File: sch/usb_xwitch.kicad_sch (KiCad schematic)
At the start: 65 parts, among them J1 USB3_A, J2 USB3_A, J3 USB3_A, J4 USB3_A, J5 USB3_A, J6 USB3_A, J7 USB3_A, J8 Conn_02x05_Odd_Even, J9 C65114, K1 Relay_DPDT_Panasonic_AGQ200A4H, K2 Relay_DPDT_Panasonic_AGQ200A4H, K3 Relay_DPDT_Panasonic_AGQ200A4H, Q1 2N7002P, Q2 2N7002P, Q3 2N7002P, SW1 C2689642, U1 Pico

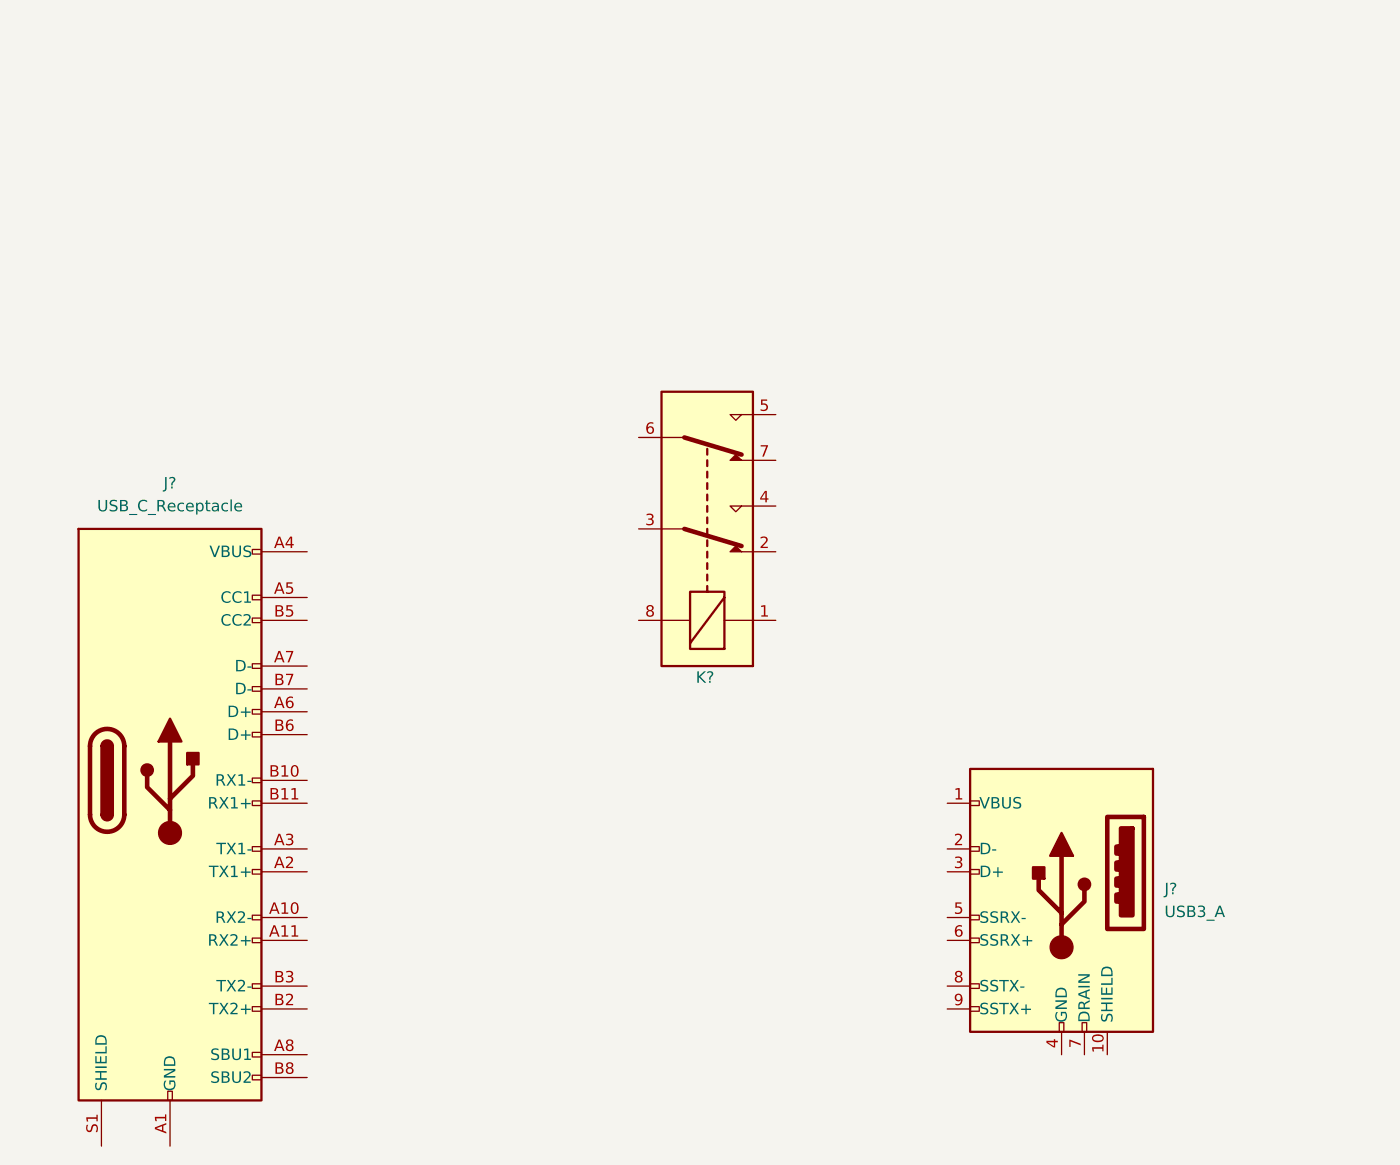
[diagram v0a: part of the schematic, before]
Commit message: added usb2 usb3 mux in sch
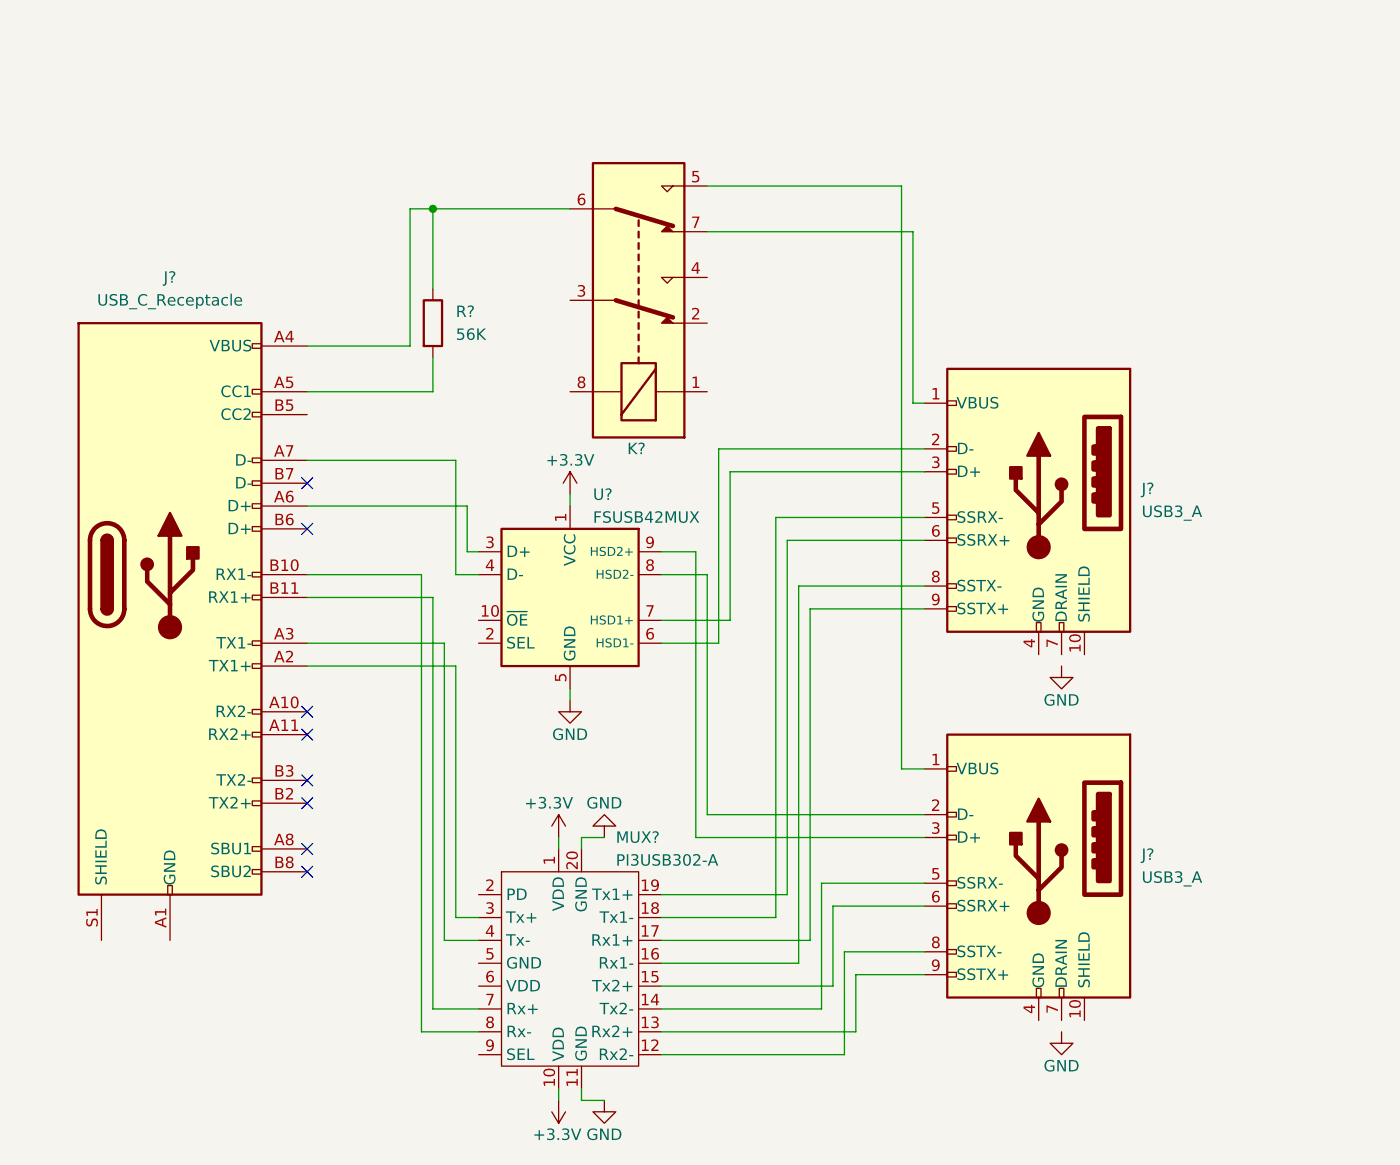
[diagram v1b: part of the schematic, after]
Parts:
- added J?: USB3_A, usb_xwitch:USB3_A_AdamTech_USB-A3-S-RA, symbol Connector:USB3_A
- added MUX?: PI3USB302-A, USB_MUX_DEMUX_PI3USB302-A:USB_MUX_DEMUX_PI3USB302-A, symbol usb_xwitch:PI3USB302-A
- added R?: 56K, symbol Device:R
- added U?: FSUSB42MUX, Package_SO:MSOP-10_3x3mm_P0.5mm, symbol Interface_USB:FSUSB42MUX
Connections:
- net +3V3: now also MUX?.1 (VDD), MUX?.10 (VDD), U?.1 (VCC)
- net GND: now also MUX?.11 (GND), MUX?.20 (GND), U?.5 (GND)
- net at K?.5: now also J?.1 (VBUS)
- net at K?.6: now also J?.A4 (VBUS), J?.A9 (VBUS), J?.B4 (VBUS), J?.B9 (VBUS), R?.1
- net at K?.7: now also J?.1 (VBUS)
- net at J?.A2 (TX1+): now also MUX?.3 (Tx+)
- net at J?.A3 (TX1-): now also MUX?.4 (Tx-)
- net at J?.A5 (CC1): now also R?.2
- net at J?.A6 (D+): now also U?.3 (D+)
- net at J?.A7 (D-): now also U?.4 (D-)
- net at J?.B10 (RX1-): now also MUX?.8 (Rx-)
- net at J?.B11 (RX1+): now also MUX?.7 (Rx+)
- net at J?.2 (D-): now also U?.6 (HSD1-)
- net at J?.3 (D+): now also U?.7 (HSD1+)
- net at J?.5 (SSRX-): now also MUX?.18 (Tx1-)
- net at J?.6 (SSRX+): now also MUX?.19 (Tx1+)
- net at J?.8 (SSTX-): now also MUX?.16 (Rx1-)
- net at J?.9 (SSTX+): now also MUX?.17 (Rx1+)
- new net: J?.2 (D-), U?.8 (HSD2-)
- new net: J?.3 (D+), U?.9 (HSD2+)
- new net: J?.5 (SSRX-), MUX?.14 (Tx2-)
- new net: J?.6 (SSRX+), MUX?.15 (Tx2+)
- new net: J?.8 (SSTX-), MUX?.12 (Rx2-)
- new net: J?.9 (SSTX+), MUX?.13 (Rx2+)
- no-connect marks 37 -> 45
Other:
- moved on the sheet: J?, K?

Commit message: updated usb mux wiring
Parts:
- added R? (x3): 0R, Resistor_SMD:R_0603_1608Metric_Pad0.98x0.95mm_HandSolder, symbol Device:R
- R?: footprint (none) -> Resistor_SMD:R_0402_1005Metric_Pad0.72x0.64mm_HandSolder; LCSC (none) -> C25796
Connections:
- net +3V3: now also MUX?.6 (VDD)
- net +5V: now also K?.1
- net GND: now also J?.A1 (GND), J?.A12 (GND), J?.B1 (GND), J?.B12 (GND), K?.3, MUX?.5 (GND), R?.1
- net PD-A: now also MUX?.2 (PD)
- net RL1: now also K?.8
- net SEL-A: now also MUX?.9 (SEL)
- net VBUS_1_1: now also J?.1 (VBUS), K?.7
- net VBUS_1_2: now also J?.1 (VBUS), K?.5
- net at K?.2: now also J?.4 (GND), J?.7 (DRAIN), R?.2
- net at K?.4: now also J?.4 (GND), J?.7 (DRAIN), R?.2
- net at J?.S1 (SHIELD): now also R?.2
- net at J?.10 (SHIELD): now also R?.1 (x2)
- no-connect marks 45 -> 46
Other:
- moved on the sheet: J6, J7, K3

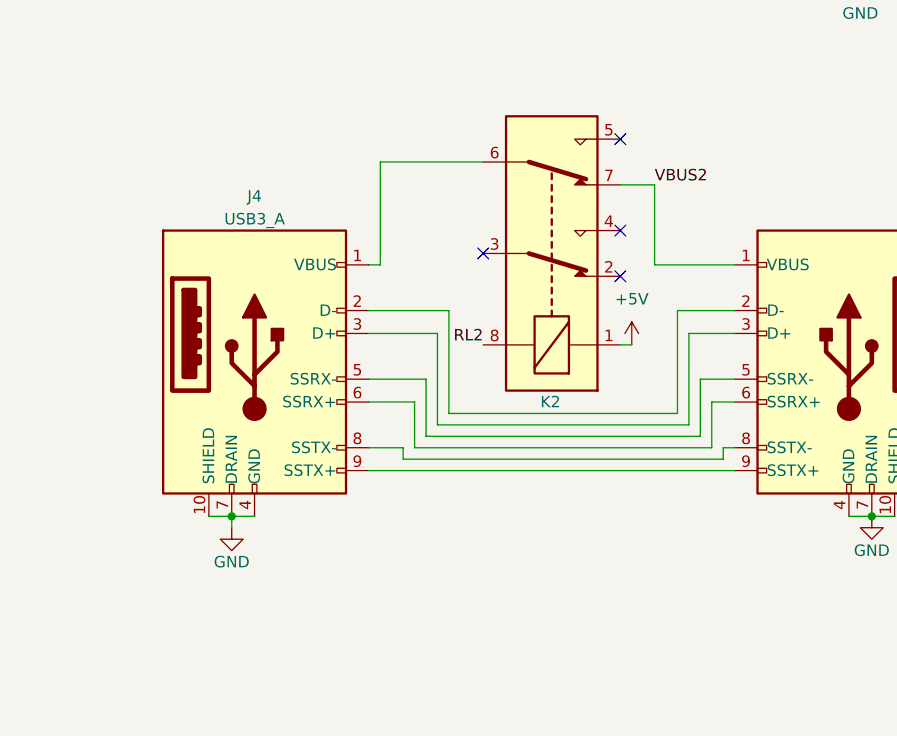
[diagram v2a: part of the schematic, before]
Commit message: added shouhan typec in lib
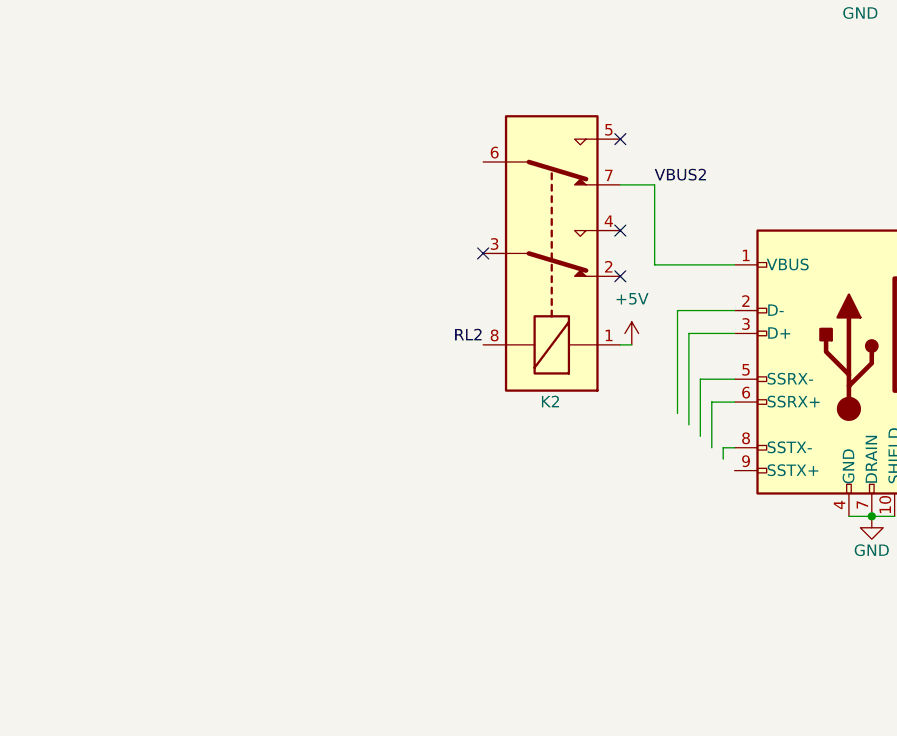
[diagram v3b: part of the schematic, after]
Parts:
- removed J4: USB3_A, usb_xwitch:USB3_A_AdamTech_USB-A3-S-RA, symbol Connector:USB3_A
- J?: footprint Connector_USB:USB_C_Receptacle_Amphenol_12401548E4-2A -> usb_xwitch:USB_TypeC_24Pin_ShouHan
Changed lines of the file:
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@@
   (junction (at 154.94 76.2) (diameter 0) (color 0 0 0 0)
   )
-  (junction (at 190.5 218.44) (diameter 0) (color 0 0 0 0)
-  )
   (junction (at 71.12 38.1) (diameter 0) (color 0 0 0 0)
   )
@@
     (stroke (width 0) (type default) (color 0 0 0 0))
   )
-  (wire (pts (xy 212.09 209.55) (xy 212.09 203.2))
-    (stroke (width 0) (type default) (color 0 0 0 0))
-  )
   (wire (pts (xy 104.14 265.43) (xy 104.14 259.08))
     (stroke (width 0) (type default) (color 0 0 0 0))
@@
     (stroke (width 0) (type default) (color 0 0 0 0))
   )
-  (wire (pts (xy 213.36 208.28) (xy 241.3 208.28))
-    (stroke (width 0) (type default) (color 0 0 0 0))
-  )
   (wire (pts (xy 237.49 77.47) (xy 257.81 77.47))
     (stroke (width 0) (type default) (color 0 0 0 0))
@@
     (stroke (width 0) (type default) (color 0 0 0 0))
   )
-  (wire (pts (xy 212.09 203.2) (xy 205.74 203.2))
-    (stroke (width 0) (type default) (color 0 0 0 0))
-  )
   (wire (pts (xy 95.25 252.73) (xy 95.25 208.28))
     (stroke (width 0) (type default) (color 0 0 0 0))
@@
     (stroke (width 0) (type default) (color 0 0 0 0))
   )
-  (wire (pts (xy 205.74 205.74) (xy 210.82 205.74))
-    (stroke (width 0) (type default) (color 0 0 0 0))
-  )
   (wire (pts (xy 176.53 86.36) (xy 171.45 86.36))
     (stroke (width 0) (type default) (color 0 0 0 0))
@@
     (stroke (width 0) (type default) (color 0 0 0 0))
   )
-  (wire (pts (xy 245.11 212.09) (xy 209.55 212.09))
-    (stroke (width 0) (type default) (color 0 0 0 0))
-  )
   (wire (pts (xy 101.6 251.46) (xy 113.03 251.46))
     (stroke (width 0) (type default) (color 0 0 0 0))
@@
     (stroke (width 0) (type default) (color 0 0 0 0))
   )
-  (wire (pts (xy 209.55 212.09) (xy 209.55 210.82))
-    (stroke (width 0) (type default) (color 0 0 0 0))
-  )
   (wire (pts (xy 151.13 60.96) (xy 148.59 60.96))
     (stroke (width 0) (type default) (color 0 0 0 0))
@@
     (stroke (width 0) (type default) (color 0 0 0 0))
   )
-  (wire (pts (xy 213.36 198.12) (xy 213.36 208.28))
-    (stroke (width 0) (type default) (color 0 0 0 0))
-  )
   (wire (pts (xy 68.58 194.31) (xy 73.66 194.31))
     (stroke (width 0) (type default) (color 0 0 0 0))
@@
     (stroke (width 0) (type default) (color 0 0 0 0))
   )
-  (wire (pts (xy 242.57 209.55) (xy 212.09 209.55))
-    (stroke (width 0) (type default) (color 0 0 0 0))
-  )
   (wire (pts (xy 83.82 212.09) (xy 87.63 212.09))
     (stroke (width 0) (type default) (color 0 0 0 0))
@@
     (stroke (width 0) (type default) (color 0 0 0 0))
   )
-  (wire (pts (xy 210.82 205.74) (xy 210.82 210.82))
-    (stroke (width 0) (type default) (color 0 0 0 0))
-  )
-  (wire (pts (xy 209.55 210.82) (xy 205.74 210.82))
-    (stroke (width 0) (type default) (color 0 0 0 0))
-  )
   (wire (pts (xy 167.64 49.53) (xy 171.45 49.53))
     (stroke (width 0) (type default) (color 0 0 0 0))
@@
     (stroke (width 0) (type default) (color 0 0 0 0))
   )
-  (wire (pts (xy 205.74 213.36) (xy 246.38 213.36))
-    (stroke (width 0) (type default) (color 0 0 0 0))
-  )
   (wire (pts (xy 83.82 219.71) (xy 91.44 219.71))
     (stroke (width 0) (type default) (color 0 0 0 0))
@@
     (stroke (width 0) (type default) (color 0 0 0 0))
   )
-  (wire (pts (xy 207.01 179.07) (xy 207.01 190.5))
-    (stroke (width 0) (type default) (color 0 0 0 0))
-  )
   (wire (pts (xy 260.35 156.21) (xy 260.35 157.48))
     (stroke (width 0) (type default) (color 0 0 0 0))
@@
     (stroke (width 0) (type default) (color 0 0 0 0))
   )
-  (wire (pts (xy 207.01 190.5) (xy 205.74 190.5))
-    (stroke (width 0) (type default) (color 0 0 0 0))
-  )
   (wire (pts (xy 62.23 207.01) (xy 62.23 212.09))
     (stroke (width 0) (type default) (color 0 0 0 0))
@@
     (stroke (width 0) (type default) (color 0 0 0 0))
   )
-  (wire (pts (xy 205.74 198.12) (xy 213.36 198.12))
-    (stroke (width 0) (type default) (color 0 0 0 0))
-  )
   (wire (pts (xy 107.95 59.69) (xy 107.95 86.36))
     (stroke (width 0) (type default) (color 0 0 0 0))
@@
     (stroke (width 0) (type default) (color 0 0 0 0))
   )
-  (wire (pts (xy 214.63 207.01) (xy 214.63 195.58))
-    (stroke (width 0) (type default) (color 0 0 0 0))
-  )
   (wire (pts (xy 62.23 212.09) (xy 63.5 212.09))
     (stroke (width 0) (type default) (color 0 0 0 0))
@@
     (stroke (width 0) (type default) (color 0 0 0 0))
   )
-  (wire (pts (xy 210.82 210.82) (xy 243.84 210.82))
-    (stroke (width 0) (type default) (color 0 0 0 0))
-  )
   (wire (pts (xy 95.25 208.28) (xy 113.03 208.28))
     (stroke (width 0) (type default) (color 0 0 0 0))
@@
     (stroke (width 0) (type default) (color 0 0 0 0))
   )
-  (wire (pts (xy 207.01 179.07) (xy 218.44 179.07))
-    (stroke (width 0) (type default) (color 0 0 0 0))
-  )
   (wire (pts (xy 60.96 25.4) (xy 71.12 25.4))
     (stroke (width 0) (type default) (color 0 0 0 0))
@@
     (stroke (width 0) (type default) (color 0 0 0 0))
   )
-  (wire (pts (xy 190.5 218.44) (xy 193.04 218.44))
-    (stroke (width 0) (type default) (color 0 0 0 0))
-  )
   (wire (pts (xy 171.45 44.45) (xy 167.64 44.45))
     (stroke (width 0) (type default) (color 0 0 0 0))
   )
-  (wire (pts (xy 240.03 207.01) (xy 214.63 207.01))
-    (stroke (width 0) (type default) (color 0 0 0 0))
-  )
   (wire (pts (xy 152.4 83.82) (xy 152.4 68.58))
     (stroke (width 0) (type default) (color 0 0 0 0))
   )
-  (wire (pts (xy 190.5 218.44) (xy 190.5 219.71))
-    (stroke (width 0) (type default) (color 0 0 0 0))
-  )
   (wire (pts (xy 90.17 222.25) (xy 90.17 200.66))
     (stroke (width 0) (type default) (color 0 0 0 0))
@@
     (stroke (width 0) (type default) (color 0 0 0 0))
   )
-  (wire (pts (xy 214.63 195.58) (xy 205.74 195.58))
-    (stroke (width 0) (type default) (color 0 0 0 0))
-  )
   (wire (pts (xy 60.96 201.93) (xy 60.96 214.63))
     (stroke (width 0) (type default) (color 0 0 0 0))
@@
     (stroke (width 0) (type default) (color 0 0 0 0))
   )
-  (wire (pts (xy 187.96 218.44) (xy 190.5 218.44))
-    (stroke (width 0) (type default) (color 0 0 0 0))
-  )
   (wire (pts (xy 128.27 68.58) (xy 121.92 68.58))
     (stroke (width 0) (type default) (color 0 0 0 0))
@@
     (property "Reference" "J?" (id 0) (at 29.21 181.61 0))
     (property "Value" "USB_C_Receptacle" (id 1) (at 29.21 184.15 0))
-    (property "Footprint" "Connector_USB:USB_C_Receptacle_Amphenol_12401548E4-2A" (id 2) (at 33.02 214.63 0)
+    (property "Footprint" "usb_xwitch:USB_TypeC_24Pin_ShouHan" (id 2) (at 33.02 214.63 0)
       (effects (font (size 1.27 1.27)) hide)
     )
@@
     (pin "1")
   )
-  (symbol (lib_id "power:GND") (at 190.5 219.71 0) (unit 1)
-    (in_bom yes) (on_board yes)
-    (property "Reference" "#PWR029" (id 0) (at 190.5 226.06 0)
-      (effects (font (size 1.27 1.27)) hide)
-    )
-    (property "Value" "GND" (id 1) (at 190.5 223.52 0))
-    (property "Footprint" "" (id 2) (at 190.5 219.71 0)
-      (effects (font (size 1.27 1.27)) hide)
-    )
-    (property "Datasheet" "" (id 3) (at 190.5 219.71 0)
-      (effects (font (size 1.27 1.27)) hide)
-    )
-    (pin "1")
-  )
   (symbol (lib_id "usb_xwitch:PI3USB302-A") (at 138.43 62.23 0) (unit 1)
     (in_bom yes) (on_board yes)
@@
     (pin "1")
   )
-  (symbol (lib_id "Connector:USB3_A") (at 193.04 200.66 0) (unit 1)
-    (in_bom yes) (on_board yes)
-    (property "Reference" "J4" (id 0) (at 193.04 182.88 0))
-    (property "Value" "USB3_A" (id 1) (at 193.04 185.42 0))
-    (property "Footprint" "usb_xwitch:USB3_A_AdamTech_USB-A3-S-RA" (id 2) (at 196.85 198.12 0)
-      (effects (font (size 1.27 1.27)) hide)
-    )
-    (property "Datasheet" "~" (id 3) (at 196.85 198.12 0)
-      (effects (font (size 1.27 1.27)) hide)
-    )
-    (pin "1")
-    (pin "10")
-    (pin "2")
-    (pin "3")
-    (pin "4")
-    (pin "5")
-    (pin "6")
-    (pin "7")
-    (pin "8")
-    (pin "9")
-  )
   (symbol (lib_id "Device:R") (at 261.62 34.29 0) (unit 1)
     (in_bom yes) (on_board yes) (fields_autoplaced)
@@
       (reference "#PWR028") (unit 1) (value "GND") (footprint "")
     )
-    (path "/57b49fdd-f3d9-4fa8-bdf1-e2e39ee38be0"
-      (reference "#PWR029") (unit 1) (value "GND") (footprint "")
-    )
     (path "/98ebec09-9bd9-48ab-a517-b8d220a08157"
       (reference "#PWR030") (unit 1) (value "GND") (footprint "")
@@
       (reference "J3") (unit 1) (value "USB3_A") (footprint "usb_xwitch:USB3_A_AdamTech_USB-A3-S-RA")
     )
-    (path "/7777c39f-7409-4ac6-aa45-921399788f7d"
-      (reference "J4") (unit 1) (value "USB3_A") (footprint "usb_xwitch:USB3_A_AdamTech_USB-A3-S-RA")
-    )
     (path "/32613975-ea2d-458f-a092-8f2ed600fa0e"
       (reference "J5") (unit 1) (value "USB3_A") (footprint "usb_xwitch:USB3_A_AdamTech_USB-A3-S-RA")
@@
     )
     (path "/4ab5c165-63d8-4329-8f05-fa2abec92f14"
-      (reference "J?") (unit 1) (value "USB_C_Receptacle") (footprint "Connector_USB:USB_C_Receptacle_Amphenol_12401548E4-2A")
+      (reference "J?") (unit 1) (value "USB_C_Receptacle") (footprint "usb_xwitch:USB_TypeC_24Pin_ShouHan")
     )
     (path "/71a687af-7ac4-4373-9578-b04c8798d7c9/5c1af89e-9217-40c2-9e2e-d6deb8e39e5e"
